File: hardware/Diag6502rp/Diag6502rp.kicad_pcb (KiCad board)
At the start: 4 copper layers, 59.5 x 54.3 mm, 72 parts, among them J1 Conn_01x21_Pin, J2 Conn_01x21_Socket, J3 Conn_01x21_Pin, J4 Conn_01x21_Socket, J5 USB4105-G-FA, J6 Conn_02x20_Counter_Clockwise, J7 Conn_ARM_SWD_TagConnect_TC2030, SW1 SW_Push, U1 TLV74311P, U10 RP2350_80QFN, U2 IP4234CZ6, U3 AP2112K-3.3, U4 TXS0108ERGYR, U5 TXS0108ERGYR, U6 TXS0108ERGYR, U7 TXS0108ERGYR, U8 TXS0108ERGYR, U9 W25Q128JVS, Y1 ABM8-272-T3

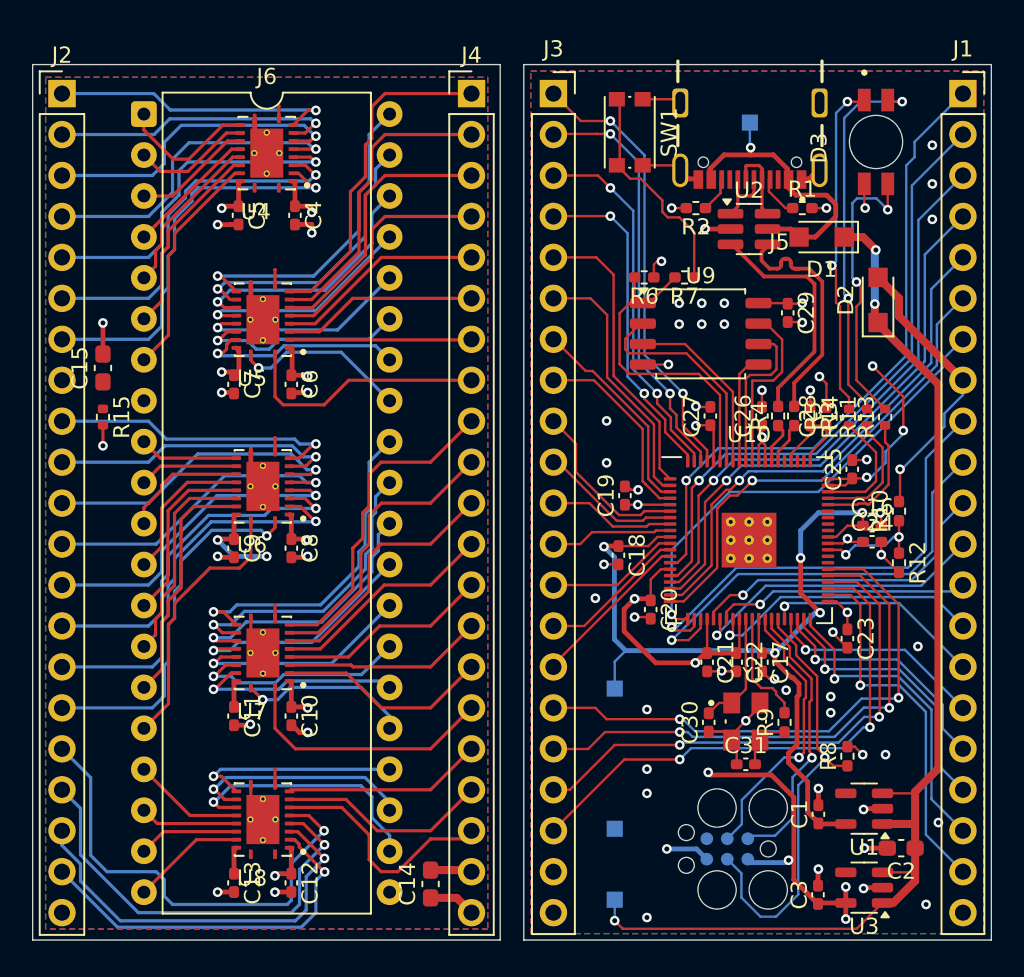
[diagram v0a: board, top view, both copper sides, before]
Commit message: Changed TSX0108e foorprint to TSSOP20 for easier routing.
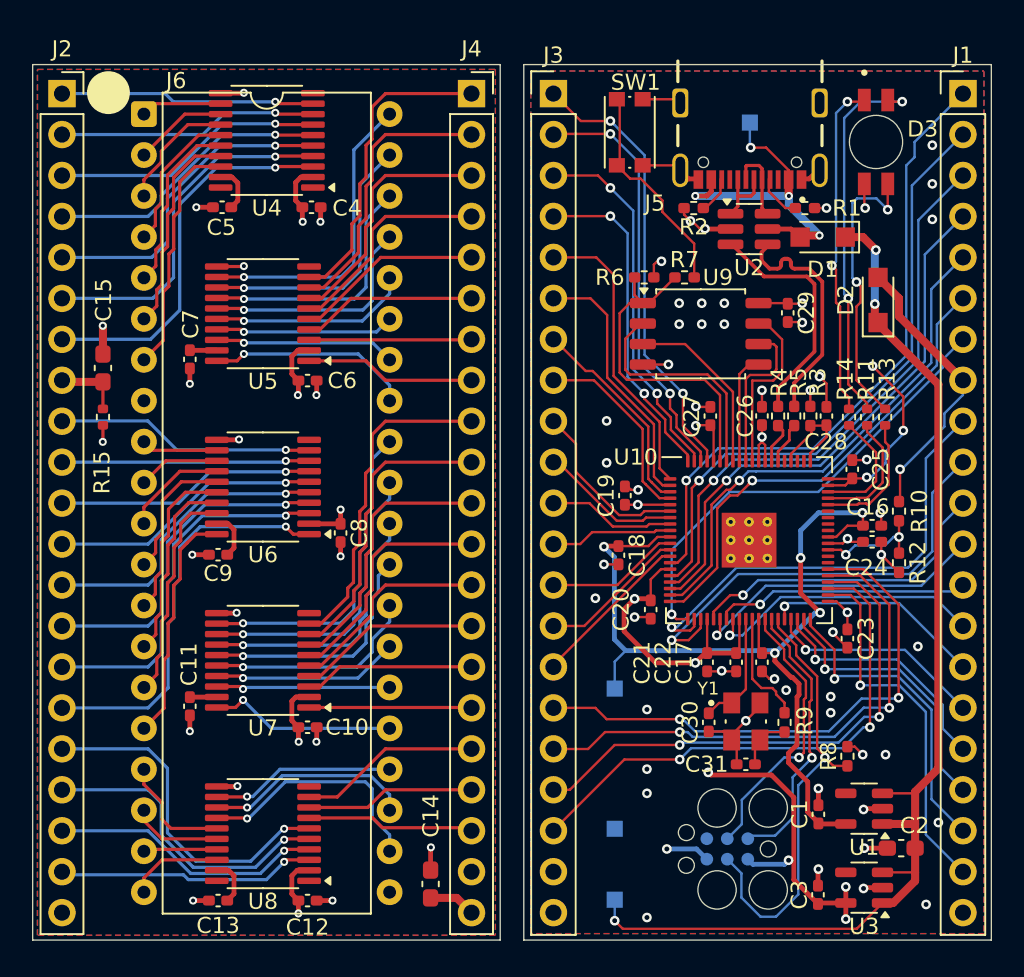
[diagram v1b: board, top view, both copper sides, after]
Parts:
- J1, J3: value Conn_01x21_Pin -> Conn_01x21_PinHeader; footprint Connector_PinSocket_2.54mm:PinSocket_1x21_P2.54mm_Vertical -> Connector_PinHeader_2.54mm:PinHeader_1x21_P2.54mm_Vertical
- J2, J4: value Conn_01x21_Socket -> Conn_01x21_PinSocket; footprint Connector_PinHeader_2.54mm:PinHeader_1x21_P2.54mm_Vertical -> Connector_PinSocket_2.54mm:PinSocket_1x21_P2.54mm_Vertical
- U4, U5, U6, U7, U8: value TXS0108ERGYR -> TXS0108EPW; footprint footprints:IC_TXS0108ERGYR -> Package_SO:TSSOP-20_4.4x6.5mm_P0.65mm
- moved C8 3.20 mm to (113.8, 65.3)
- moved C7 3.15 mm to (104.5, 54.6)
- moved C11 2.80 mm to (104.5, 76.1)
- moved C12 1.49 mm to (111.8, 88.2), turned to 0 degrees
- moved C13 1.48 mm to (106.2, 88.2), turned to 180 degrees
- moved C10 1.22 mm to (111.8, 77.4), turned to 0 degrees
- moved C4 1.14 mm to (112.0, 45.1), turned to 0 degrees
- moved C5 1.14 mm to (106.5, 45.1), turned to 180 degrees
- moved C9 1.07 mm to (106.2, 66.7), turned to 180 degrees
- moved C6 1.03 mm to (111.8, 55.9), turned to 0 degrees
- moved U8 0.87 mm to (109.0, 84.0)
- moved U4 0.79 mm to (109.2, 41.0)
- moved U7 0.46 mm to (109.0, 73.2)
- moved U5 0.38 mm to (109.0, 51.8)
- moved R1 0.16 mm to (142.6, 45.2)
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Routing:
- net /Level Shifters & CPU Interface/CPU_19: track 25.4 -> 17.0 mm
- net /Level Shifters & CPU Interface/GND_I: track 29.1 -> 20.8 mm, vias 12 -> 18
- net /Level Shifters & CPU Interface/CPU_17: track 29.4 -> 21.4 mm
- net /Level Shifters & CPU Interface/CPU_18: track 26.9 -> 19.2 mm
- net /Level Shifters & CPU Interface/CPU_20: track 23.4 -> 15.8 mm
- net /Level Shifters & CPU Interface/CPU_25: track 16.3 -> 10.0 mm
- net /Level Shifters & CPU Interface/CPU_33: track 15.7 -> 10.6 mm
- net /Level Shifters & CPU Interface/CPU_22: track 14.9 -> 10.1 mm
- net /Level Shifters & CPU Interface/PIN_1: track 8.58 -> 4.11 mm
- net /Level Shifters & CPU Interface/+3V3_I: track 16.7 -> 21.0 mm
- net /Level Shifters & CPU Interface/CPU_11: track 19.2 -> 16.1 mm
- net /Level Shifters & CPU Interface/+5V_I: track 19.2 -> 16.2 mm, vias 4 -> 0
- net /Level Shifters & CPU Interface/CPU_10: track 18.3 -> 15.4 mm
- net /Level Shifters & CPU Interface/CPU_3: track 19.6 -> 16.9 mm
- net /Level Shifters & CPU Interface/CPU_26: track 13.2 -> 10.6 mm
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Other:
- board text added: "GND"

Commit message: Main design completed
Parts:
- added IF_Board: Board, PCM_kikit:Board, F.Cu at (94.7, 36.3)
- added J10: Conn_01x20_Pin, Connector_PinHeader_2.54mm:PinHeader_1x20_P2.54mm_Vertical, B.Cu at (116.8, 86.4)
- added J11: Conn_01x20_Pin, Connector_PinHeader_2.54mm:PinHeader_1x20_P2.54mm_Vertical, B.Cu at (101.6, 86.4)
- added J8: Conn_01x02_Socket, Connector_PinSocket_2.54mm:PinSocket_1x02_P2.54mm_Vertical, F.Cu at (116.8, 88.9)
- added J9: Conn_01x02_Pin, Connector_PinHeader_2.54mm:PinHeader_1x02_P2.54mm_Vertical, F.Cu at (132.1, 88.9)
- added REF**: Board, PCM_kikit:Board, F.Cu at (166.0, 35.9)
- added REF**: Untitled, footprints:SaD Logo, B.Cu at (135.3, 51.9)
- J1, J3: value Conn_01x21_PinHeader -> Conn_01x20_PinHeader; footprint Connector_PinHeader_2.54mm:PinHeader_1x21_P2.54mm_Vertical -> Connector_PinHeader_2.54mm:PinHeader_1x20_P2.54mm_Vertical
- J2: footprint Connector_PinSocket_2.54mm:PinSocket_1x21_P2.54mm_Vertical -> Connector_PinSocket_2.54mm:PinSocket_1x20_P2.54mm_Vertical
- J4: value Conn_01x21_PinSocket -> Conn_01x20_PinSocket; footprint Connector_PinSocket_2.54mm:PinSocket_1x21_P2.54mm_Vertical -> Connector_PinSocket_2.54mm:PinSocket_1x20_P2.54mm_Vertical
- moved TP1 17.0 mm to (140.6, 88.9)
- moved TP3 12.0 mm to (142.7, 88.9)
- moved TP4 9.23 mm to (138.4, 88.9)
- moved C14 5.35 mm to (114.3, 85.4)
- moved J7 4.73 mm to (133.3, 83.3), turned to 90 degrees
- moved C12 1.28 mm to (110.5, 88.4), turned to 180 degrees
- moved J6 1.27 mm to (101.6, 38.1)
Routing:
- net +3V3: track 86.1 -> 68.3 mm, vias 21 -> 20
- net /Power Supply & USB/V_{SUP}: track 71.1 -> 58.4 mm
- net /Processor/SWDIO: track 17.0 -> 25.6 mm, vias 1 -> 3
- net +1V1: track 56.7 -> 60.8 mm, vias 5 -> 6
- net /Processor/SWCLK: track 17.2 -> 20.6 mm, vias 1 -> 3
- net /Processor/A12: track 32.9 -> 35.0 mm
- net /Level Shifters & CPU Interface/PIN_20: track 5.87 -> 3.79 mm
- net /Level Shifters & CPU Interface/CPU_9: track 16.1 -> 18.1 mm
- net /Level Shifters & CPU Interface/PIN_22: track 15.1 -> 13.1 mm
- net /Level Shifters & CPU Interface/CPU_33: track 10.6 -> 12.5 mm
- net /Level Shifters & CPU Interface/CPU_5: track 20.0 -> 21.9 mm
- net /Level Shifters & CPU Interface/CPU_18: track 19.2 -> 21.1 mm
- net /Level Shifters & CPU Interface/CPU_19: track 17.0 -> 18.9 mm
- net /Level Shifters & CPU Interface/CPU_7: track 23.8 -> 25.6 mm
- net /Level Shifters & CPU Interface/GND_I: track 20.8 -> 22.6 mm, vias 18 -> 17
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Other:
- board text added: "6502 I/F Rev.A 2025/30"
- board text added: "6502 I/F-Board Rev.A 2025/30"
- board text added: "6502DIAG"
- board text added: "Rev.A 2025/30"
- board text added: "USB BOOT"

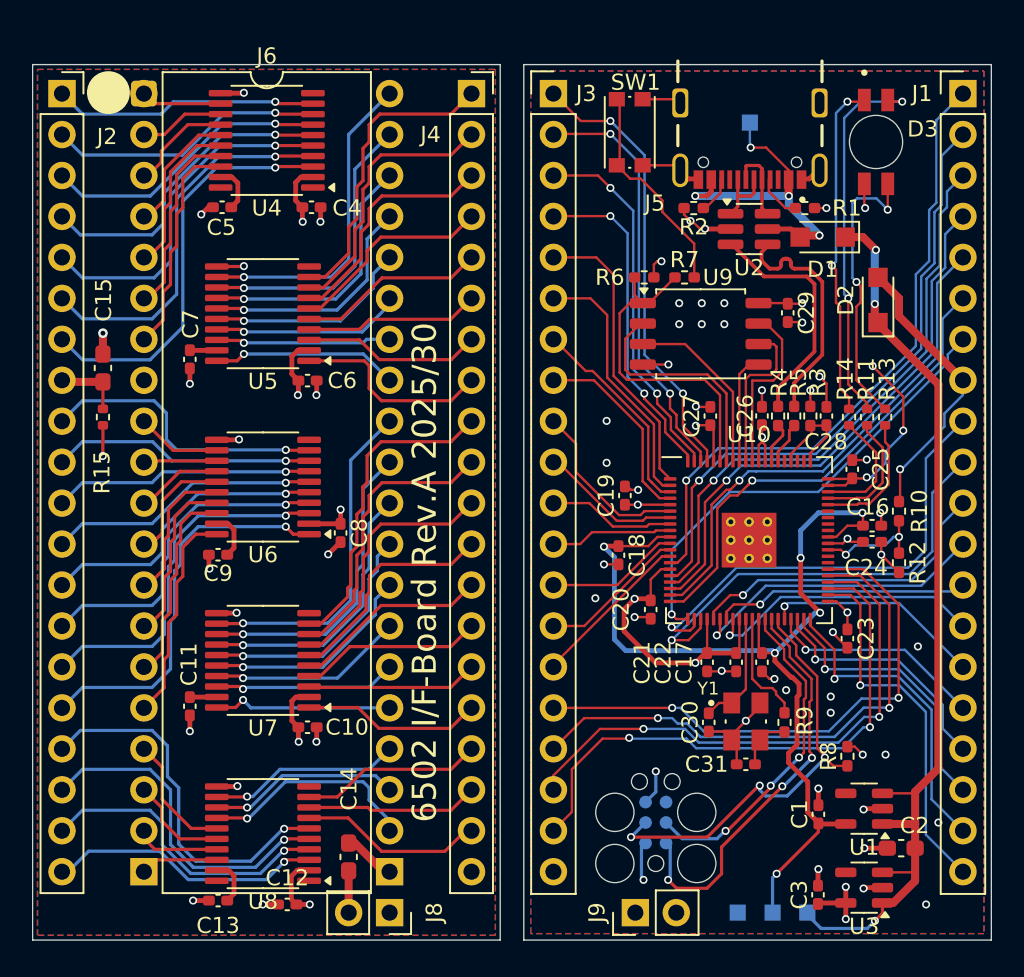
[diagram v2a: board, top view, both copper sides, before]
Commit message: Cleanup, Fiduciaries, component spacing
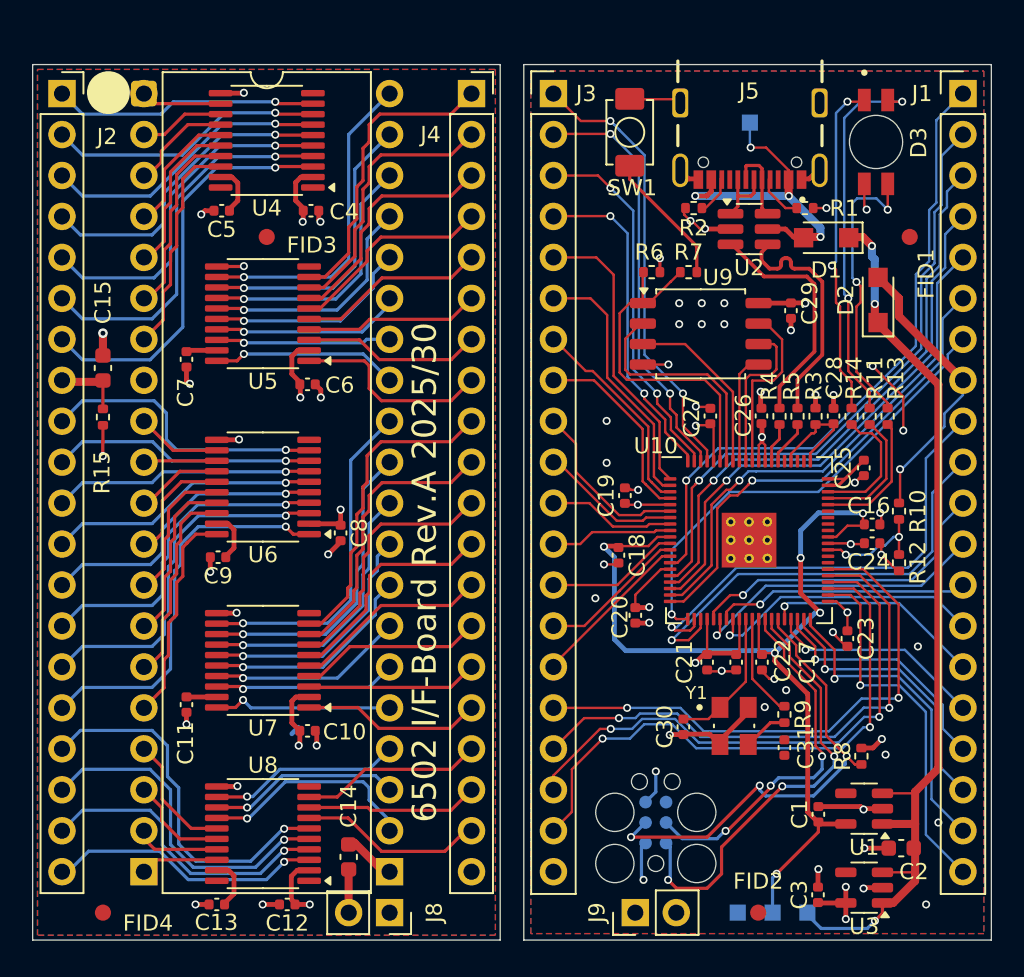
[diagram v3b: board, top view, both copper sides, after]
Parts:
- added FID1: Fiducial, Fiducial:Fiducial_1mm_Mask2mm, F.Cu at (149.1, 47.0)
- added FID2: Fiducial, Fiducial:Fiducial_1mm_Mask2mm, F.Cu at (139.7, 88.9)
- added FID3: Fiducial, Fiducial:Fiducial_1mm_Mask2mm, F.Cu at (109.2, 47.0)
- added FID4: Fiducial, Fiducial:Fiducial_1mm_Mask2mm, F.Cu at (99.1, 88.9)
- C1, C10, C11, C12, C13, C16, C17, C18, C19, C20, C21, C22, C23, C24, C25, C26, C27, C28, C29, C3, C30, C31, C4, C5, C6, C7, C8, C9: footprint Capacitor_SMD:C_0402_1005Metric_Pad0.74x0.62mm_HandSolder -> Capacitor_SMD:C_0402_1005Metric
- C14, C15, C2: footprint Capacitor_SMD:C_0603_1608Metric_Pad1.08x0.95mm_HandSolder -> Capacitor_SMD:C_0603_1608Metric
- J10, J11: value Conn_01x20_Pin -> Conn_01x20_PinHeader
- J2: value Conn_01x21_PinSocket -> Conn_01x20_PinSocket
- J5: value USB4105-G-FA -> USB4105-GF-A-120
- J8: value Conn_01x02_Socket -> Conn_01x02_PinSocket
- J9: value Conn_01x02_Pin -> Conn_01x02_PinHeader
- R1, R10, R12, R2, R3, R4, R5, R6, R7, R8, R9: footprint Resistor_SMD:R_0402_1005Metric_Pad0.72x0.64mm_HandSolder -> Resistor_SMD:R_0402_1005Metric
- SW1: value SW_Push -> TS-1088-AR02016; footprint Button_Switch_SMD:SW_Push_1P1T_NO_CK_KMR2 -> footprints:TS-1088-xxxxxxx
- U1: value TLV74311P -> TLV74311PDBVR
- U4, U5, U6, U7, U8: value TXS0108EPW -> TXS0108EPWR
- moved B2 31.1 mm to (136.5, 26.1)
- moved C31 2.61 mm to (141.3, 78.7), turned to 90 degrees
- moved C30 1.60 mm to (135.1, 77.4)
- moved C20 1.02 mm to (132.1, 70.5)
- moved R8 0.87 mm to (146.1, 79.2)
- moved Y1 0.78 mm to (138.2, 77.3)
- moved B1 0.76 mm to (95.5, 36.3)
- moved C25 0.72 mm to (146.3, 61.3), turned to -90 degrees
- moved R6 0.57 mm to (133.1, 49.2)
- moved R9 0.49 mm to (141.3, 76.6)
- moved C28 0.44 mm to (144.4, 58.1)
- moved R7 0.41 mm to (135.4, 49.2)
- moved R3 0.32 mm to (143.3, 58.1)
- moved C13 0.25 mm to (106.1, 88.4)
- moved C29 0.24 mm to (141.7, 51.6)
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- renumbered IF_Board to B1, REF** to B2
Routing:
- net +3V3: track 68.3 -> 55.2 mm, vias 20 -> 19
- net Net-(R7-Pad1): track 13.1 -> 8.32 mm
- net /Processor/SWCLK: track 20.6 -> 22.8 mm
- net /Processor/SWDIO: track 25.6 -> 27.8 mm
- net /Processor/RUN: track 27.5 -> 29.1 mm
- net /Processor/XIN: track 7.24 -> 8.71 mm
- net GND: track 44.2 -> 42.9 mm, vias 38 -> 36
- net /Level Shifters & CPU Interface/+5V_I: track 16.2 -> 16.9 mm
- net /Level Shifters & CPU Interface/+3V3_I: track 20.9 -> 21.6 mm
- net /Processor/VREG_AVDD: track 6.28 -> 6.99 mm
- net /Processor/A12: track 35.0 -> 35.7 mm
- net /Processor/~{RGB_R}: track 7.41 -> 8.07 mm
- net /Processor/XOUT: track 7.03 -> 6.40 mm
- net +1V1: track 60.8 -> 60.2 mm
- net /Processor/QSPI_SS: track 20.3 -> 20.9 mm
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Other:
- board text added: "DIAG6502"
- board text removed: "6502DIAG"

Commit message: preparing for assembly
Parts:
- J5: value USB4105-GF-A-120 -> GT-USB-7010AN
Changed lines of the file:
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@@
 			)
 		)
-		(property "Description" ""
+		(property "Description" "Fiducial Marker"
 			(at 0 0 0)
 			(layer "F.Fab")
@@
 			)
 		)
-		(property "Value" "USB4105-GF-A-120"
+		(property "Value" "GT-USB-7010AN"
 			(at 5.16 -7.135 180)
 			(layer "F.Fab")
@@
 			)
 		)
+		(property "LCSC" "C963370"
+			(at 0 0 0)
+			(layer "F.SilkS")
+			(hide yes)
+			(effects
+				(font
+					(size 1.27 1.27)
+					(thickness 0.15)
+				)
+			)
+		)
 		(property ki_fp_filters "USB*C*Receptacle*")
 		(sheetname "/Power Supply & USB/")
@@
 			)
 		)
-		(property "Description" ""
+		(property "Description" "Push button switch, generic, two pins"
+			(at 0 0 270)
+			(unlocked yes)
+			(layer "F.Fab")
+			(hide yes)
+			(effects
+				(font
+					(size 1 1)
+					(thickness 0.15)
+				)
+			)
+		)
+		(property "LCSC Part #" "C720477"
+			(at 0 0 270)
+			(unlocked yes)
+			(layer "F.Fab")
+			(hide yes)
+			(effects
+				(font
+					(size 1 1)
+					(thickness 0.15)
+				)
+			)
+		)
+		(property "Mouser Part #" ""
+			(at 0 0 270)
+			(unlocked yes)
+			(layer "F.Fab")
+			(hide yes)
+			(effects
+				(font
+					(size 1 1)
+					(thickness 0.15)
+				)
+			)
+		)
+		(property "LCSC Name" ""
 			(at 0 0 270)
 			(unlocked yes)
@@
 			)
 		)
-		(property "Description" ""
+		(property "Description" "Fiducial Marker"
 			(at 0 0 0)
 			(layer "F.Fab")
@@
 		(sheetname "/Level Shifters & CPU Interface/")
 		(sheetfile "cpu_interface.kicad_sch")
-		(attr through_hole exclude_from_bom allow_missing_courtyard dnp)
+		(attr through_hole exclude_from_pos_files exclude_from_bom allow_missing_courtyard
+			dnp
+		)
 		(fp_line
 			(start 1.16 -1.33)
@@
 			)
 		)
-		(property "Description" ""
+		(property "Description" "Fiducial Marker"
 			(at 0 0 0)
 			(layer "F.Fab")
@@
 			)
 		)
-		(property "Description" ""
+		(property "Description" "Fiducial Marker"
 			(at 0 0 0)
 			(layer "F.Fab")
